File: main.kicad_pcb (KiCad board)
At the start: 4 copper layers, 100 x 100 mm, 71 parts, among them J101 Conn_Coaxial, J201 Conn_ARM_JTAG_SWD_10, J202 Conn_02x10_Row_Letter_First, Q501 2N7002, Q601 2N7002, Q701 2N7002, U101 SA818V, U201 STM32F302CBTx, U202 CAT24C32, U203 TLV73333PQDBVRQ1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

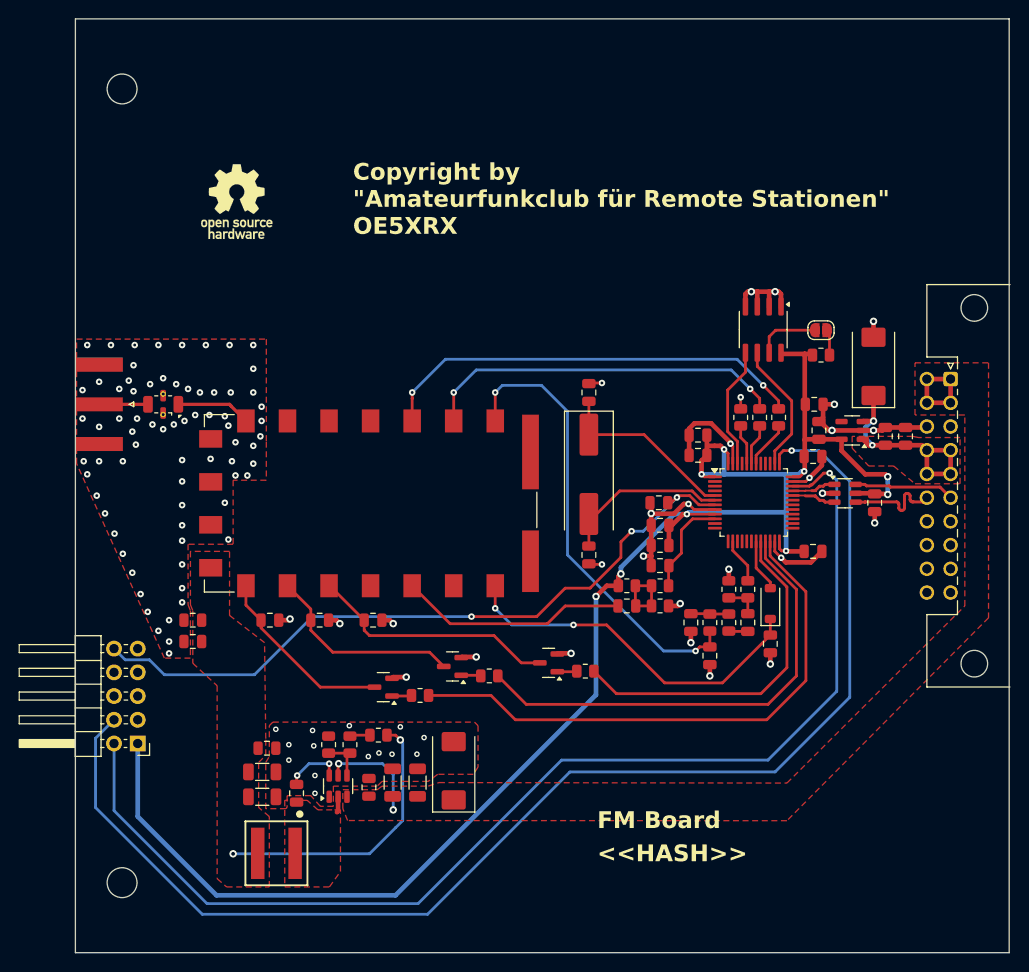
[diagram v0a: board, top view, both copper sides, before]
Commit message: update stm32, add some new 3d files
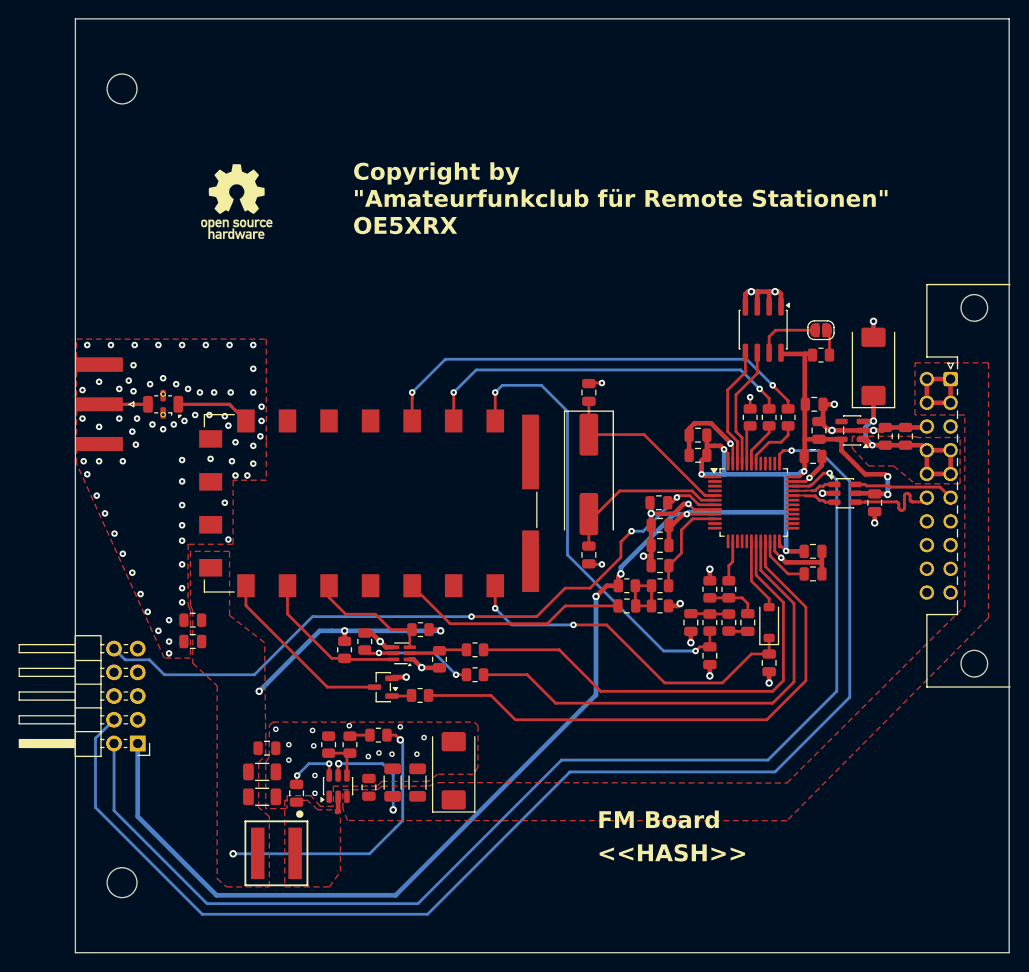
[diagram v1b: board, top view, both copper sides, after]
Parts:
- removed C501, C601, C701: 10nF/NP0, Capacitor_SMD:C_0805_2012Metric
- removed Q601: 2N7002, Package_TO_SOT_SMD:SOT-23
- removed R601: 10k, Resistor_SMD:R_0805_2012Metric
- added C216: 4.7u/10V/X5R, Capacitor_SMD:C_0805_2012Metric, F.Cu at (176.9, 95.7)
- added R702: 4k7, Resistor_SMD:R_0805_2012Metric, F.Cu at (140.7, 106.5)
- added R703: 47k, Resistor_SMD:R_0805_2012Metric, F.Cu at (134.9, 101.7)
- added R704: 47k, Resistor_SMD:R_0805_2012Metric, F.Cu at (126.7, 103.8)
- added R705: 100k, Resistor_SMD:R_0805_2012Metric, F.Cu at (128.9, 102.9)
- added R706: 100k, Resistor_SMD:R_0805_2012Metric, F.Cu at (136.9, 104.9)
- Q701: value 2N7002 -> BC847BS; footprint Package_TO_SOT_SMD:SOT-23 -> Package_TO_SOT_SMD:SOT-363_SC-70-6
- R701: value 10k -> 4k7
- U201: value STM32F302CBTx -> STM32U575CITx
- moved Q701 5.64 mm to (132.8, 104.2)
- moved R701 3.18 mm to (140.7, 103.8)
- moved C103 2.04 mm to (172.2, 105.2)
- moved D101 2.04 mm to (172.2, 100.9)
- moved R302 2.03 mm to (165.9, 97.4)
- moved R301 2.03 mm to (167.9, 97.4)
- moved R201 1.02 mm to (170.2, 78.9)
- moved R101 1.02 mm to (174.2, 78.9)
- moved R102 1.02 mm to (172.2, 78.9)
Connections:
- net Net-(U201-BOOT0) renamed /Connector and CPU/BOOT0
- Q701 pad 1: Net-(Q701-G) -> GND
- Q701 pad 2: GND -> Net-(Q701A-B1)
- Q701 pad 3: /nPOWER_DOWN -> /nPTT
- R701 pad 2: Net-(Q701-G) -> Net-(Q701A-B1)
- U201 pad 18: unconnected-(U201-PB0-Pad18) -> /Connector and CPU/GPIO4
- U201 pad 19: /Connector and CPU/GPIO4 -> /GPIO2
- U201 pad 21: /GPIO2 -> /GPIO3
- U201 pad 22: /GPIO3 -> Net-(U201-VCAP)
- U201 pad 26: unconnected-(U201-PB13-Pad26) -> /Connector and CPU/I2C_SCL
- U201 pad 27: unconnected-(U201-PB14-Pad27) -> /Connector and CPU/I2C_SDA
- U201 pad 30: /Connector and CPU/I2C_SCL -> unconnected-(U201-PA9-Pad30)
- U201 pad 31: /Connector and CPU/I2C_SDA -> unconnected-(U201-PA10-Pad31)
- U201 pad 38: /Connector and CPU/I2C_SCL_MEM -> unconnected-(U201-PA15-Pad38)
- U201 pad 45: unconnected-(U201-PB8-Pad45) -> /Connector and CPU/I2C_SCL_MEM
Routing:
- net +5V_HF: track 30.2 -> 54.7 mm, vias 2 -> 5
- net /GPIO1: track 37.5 -> 52.0 mm
- net Net-(Q701B-B2): track 0.00 -> 13.5 mm, vias 0 -> 2
- net /nPTT: track 26.6 -> 13.6 mm
- net Net-(Q701A-B1): track 0.00 -> 6.23 mm
- net Net-(U201-VCAP): track 0.00 -> 6.00 mm
- net /nPOWER_DOWN: track 21.6 -> 15.7 mm
- net /Connector and CPU/GPIO4: track 5.64 -> 7.83 mm
- net Net-(Q701-G): track 2.11 -> 0.00 mm
- net Net-(Q601-G): track 2.11 -> 0.00 mm
- net GND: track 86.6 -> 88.6 mm, vias 114 -> 111
- net Net-(C301-Pad2): track 3.73 -> 5.40 mm
- net /Connector and CPU/USART_TX: track 5.06 -> 6.20 mm
- net /RADIO_TX: track 39.2 -> 40.2 mm
- net /RADIO_RX: track 46.4 -> 47.5 mm
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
